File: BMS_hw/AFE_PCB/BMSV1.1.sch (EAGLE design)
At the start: 272 parts, among them IC1 MC33771BEP, IC2 SFH6156-1, IC3 MIC28515V1, IC4 FOD8384-COC, IC5 FOD8384-COC, IC6 FOD8384-COC, IC7 SFH6156-1, IC8 SFH6156-1, Q1 IRLML5203, Q2 IRLML5203, T1 IPT020N10N3V1, T2 IPT020N10N3V1, T3 IPT020N10N3V1, T4 IPT020N10N3V1, U1 NCP1117LP-PG, U2 NCP1117LP-PG, X5 22-23-2041

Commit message: itt@21
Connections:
- net CB_14+/14_C: now also C63.2, C64.2, C80.2, C86.2, IC3.VIN, IC3.VIN@1, IC3.VIN@2, IC3.VIN@3, IC3.VIN@4, IC3.VIN@5, IC3.VIN@6, R79.1
- net VIN: no longer C63.2, C64.2, C80.2, C86.2, IC3.VIN, IC3.VIN@1, IC3.VIN@2, IC3.VIN@3, IC3.VIN@4, IC3.VIN@5, IC3.VIN@6, R79.1

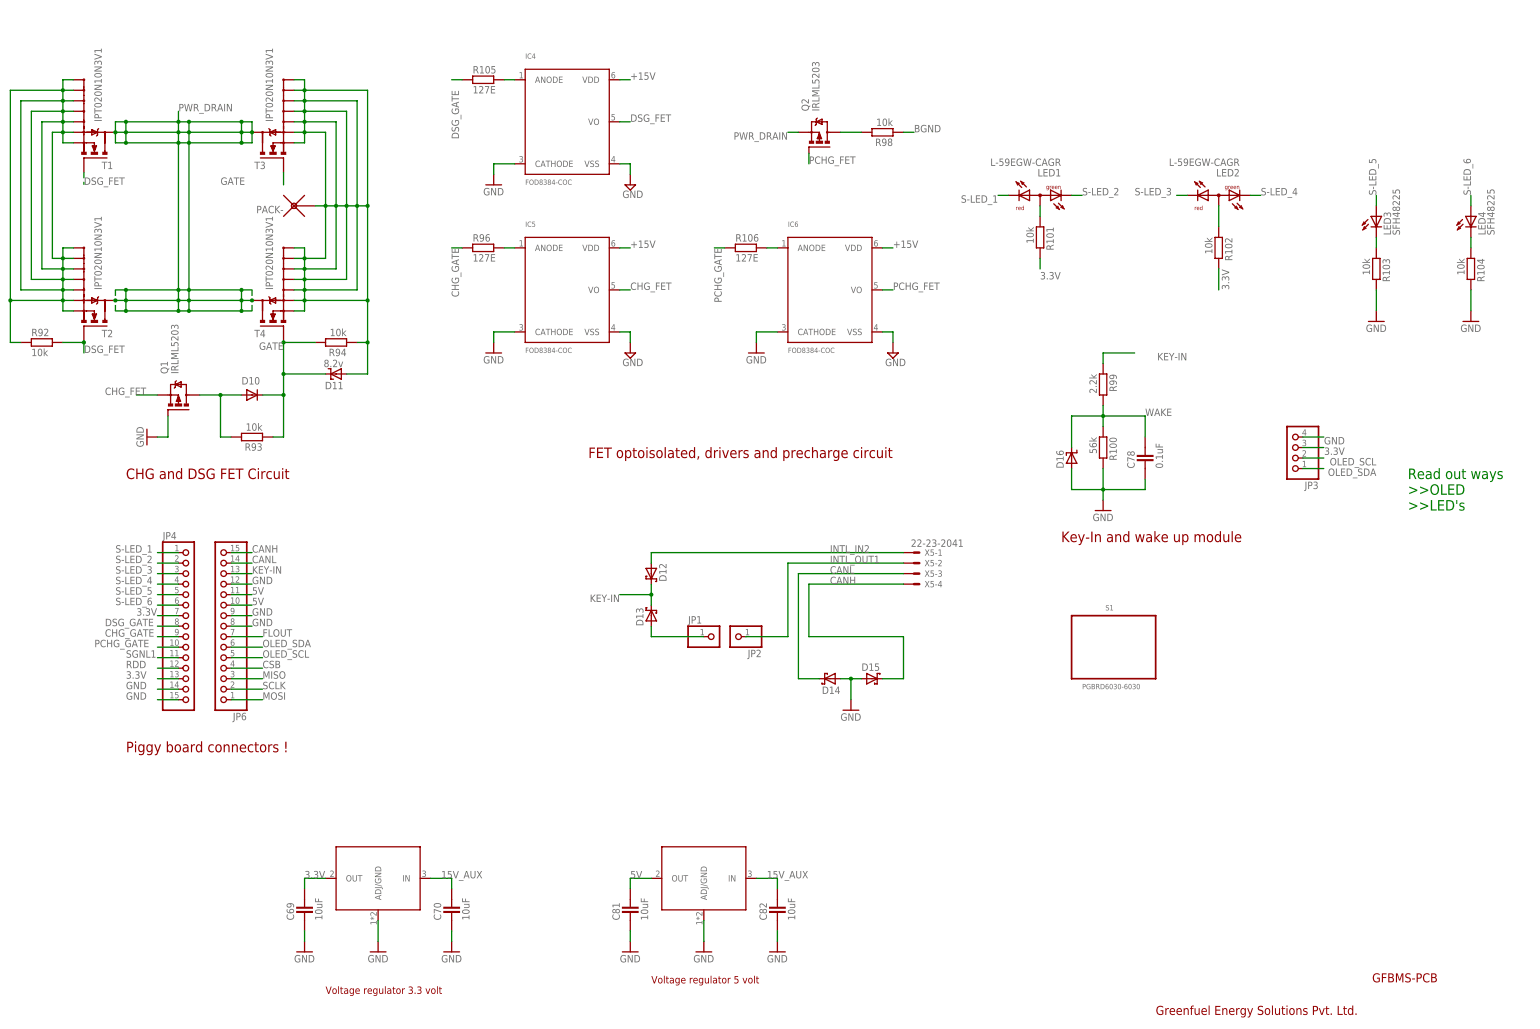
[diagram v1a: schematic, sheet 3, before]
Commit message: updated sch with diff AFE version1.1
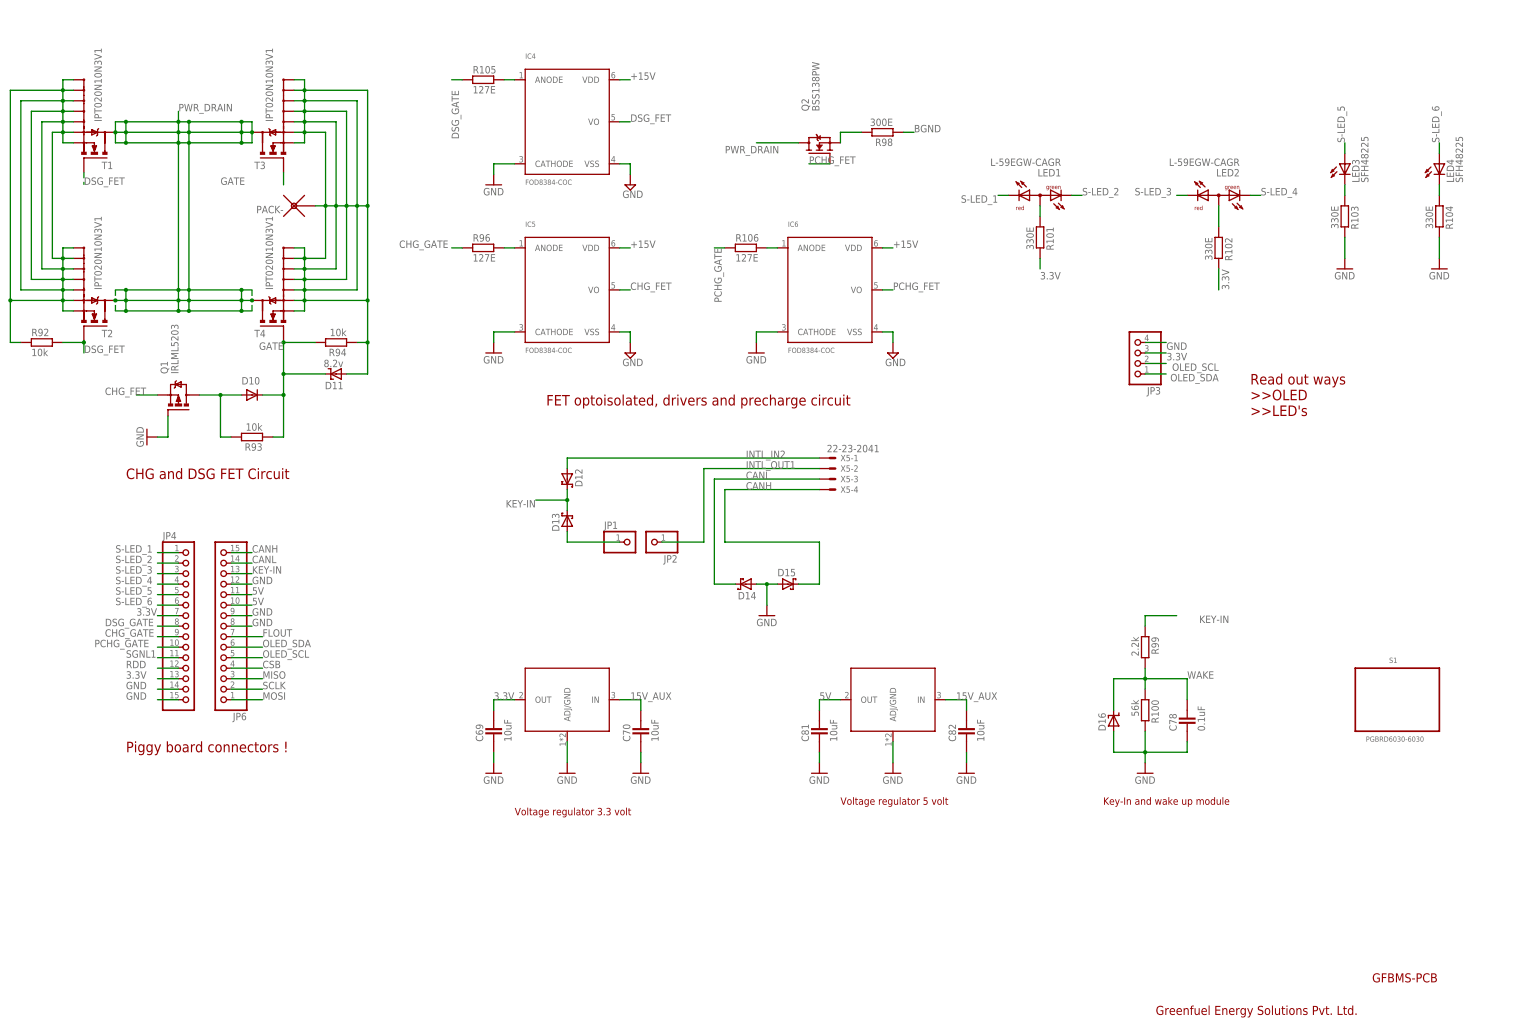
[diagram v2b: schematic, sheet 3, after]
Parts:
- added C90: 39uF 100V, ipc-7351-capacitor:POLARISED_CASE_B
- added C91: 330uF 25V, ipc-7351-capacitor:POLARISED_CASE_B
- Q2: value IRLML5203 -> BSS138PW; device transistor-power:IRLML5203 -> simpa:BSS138PW
- R101, R102, R103, R104: value 10k -> 330E
- R98: value 10k -> 300E
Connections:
- removed net SGNL: D21.A
- net CB_14+/14_C: now also C90.+, IC7LED.K
- net GND: now also C90.-, C91.-, D21.A; no longer IC7LED.K
- net N$28: now also Q2.S; no longer Q2.D
- net PWR_DRAIN: now also Q2.D; no longer Q2.S
- net VCC: now also C91.+
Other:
- moved on the sheet: C69, C70, C78, C81, C82, D12, D13, D14, D15, D16, JP1, JP2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

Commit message: replace part with fod8384 with tlp152 added datasheet in doc folder
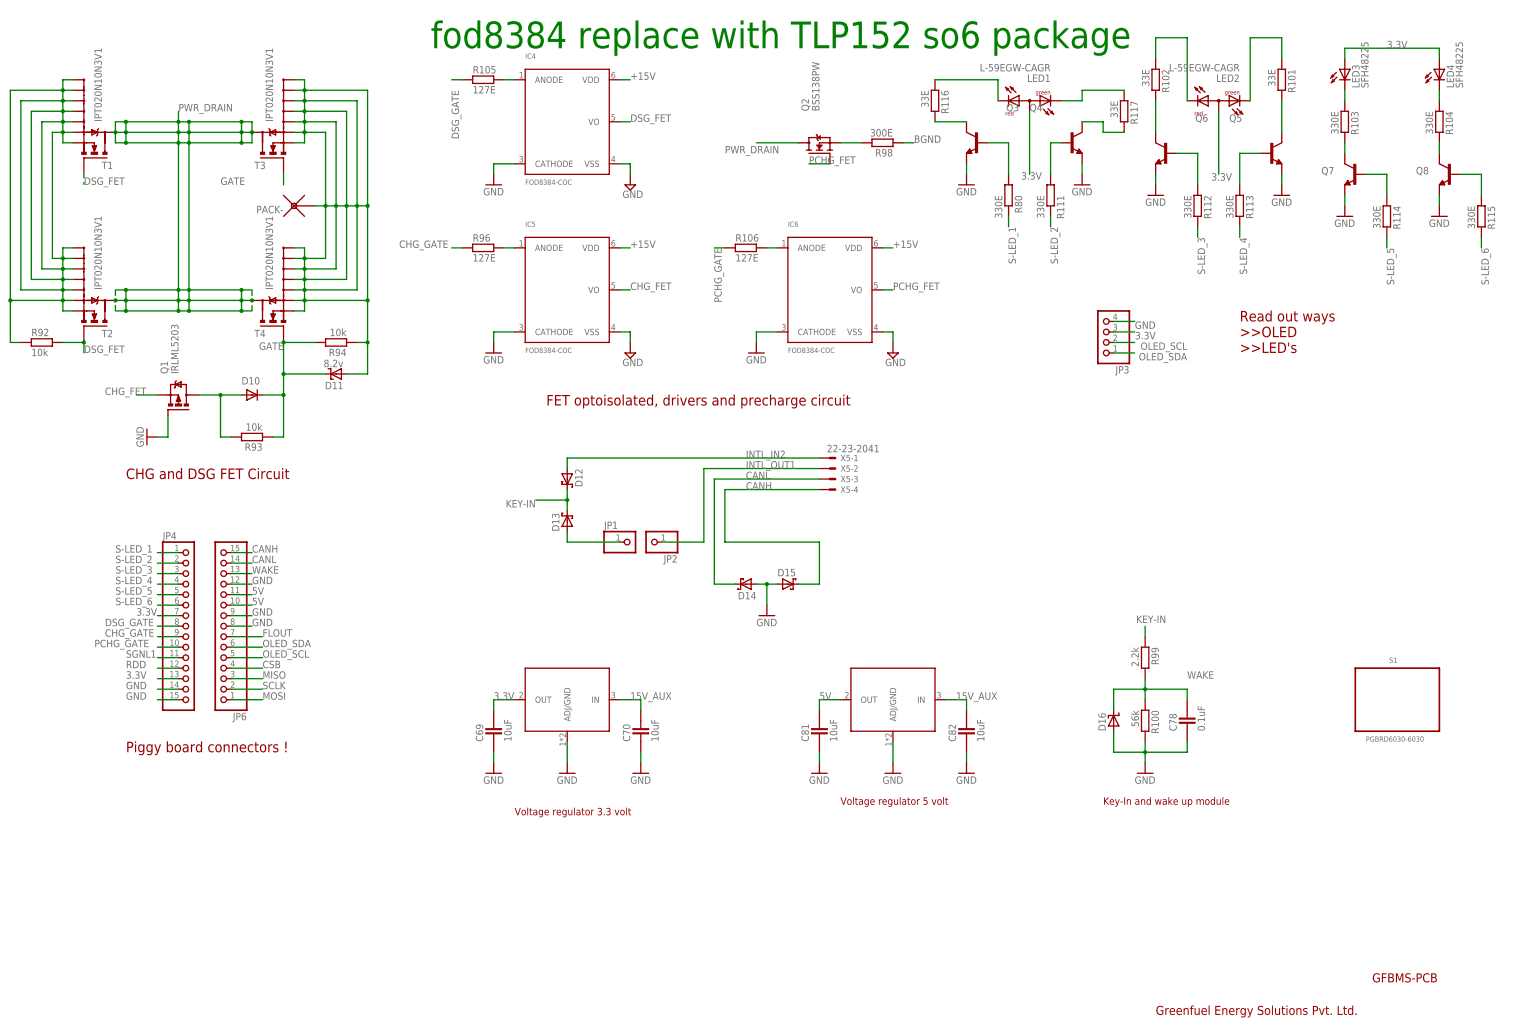
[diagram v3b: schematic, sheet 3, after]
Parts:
- removed C80, C86: 2.2uF 100V, ipc-7351-capacitor:CAPACITOR_1210
- added Q3, Q4, Q5, Q6, Q7, Q8: (no value), ipc-7351-transistor:NPN_SOT-23
- added R111, R112, R113, R114, R115: 330E, ipc-7351-resistor:RESISTOR_0402
- added R116, R117: 33E, ipc-7351-resistor:RESISTOR_0402
- added R118: 0E, ipc-7351-resistor:RESISTOR_0402
- C66: value 47nF -> 0.1uF 100V
- C73: value 1uF -> 2.2uF 16V
- C78: device ipc-7351-capacitor:CAPACITOR_0402 -> ipc-7351-capacitor:CAPACITOR_0603
- C81, C82: device ipc-7351-capacitor:CAPACITOR_0603 -> ipc-7351-capacitor:CAPACITOR_0402
- D16: device ipc-7351-diode:ZENER_SOD-123 -> ipc-7351-diode:ZENER_SOD-323
- R101, R102: value 330E -> 33E
- R66: value 10 -> 10R; device ipc-7351-resistor:RESISTOR_0402 -> ipc-7351-resistor:RESISTOR_0603
- R7: value 100 -> 39E
- R79: value 127E -> 2E
- R80: value 1.6k -> 330E; device ipc-7351-resistor:RESISTOR_0603 -> ipc-7351-resistor:RESISTOR_0402
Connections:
- removed net N$71: LED1.A, R101.1
- removed net N$74: LED2.A, R102.1
- new net N$22: Q7.C, R103.2
- new net N$29: Q8.C, R104.2
- new net N$32: Q3.B, R80.1
- new net N$37: Q4.B, R111.1
- new net N$39: Q6.B, R112.1
- new net N$40: Q5.B, R113.1
- new net N$42: Q7.B, R114.1
- new net N$43: Q8.B, R115.1
- new net N$44: LED1.CR, R116.1
- new net N$45: Q3.C, R116.2
- new net N$47: LED1.CG, R117.1
- new net N$56: Q6.C, R102.2
- new net N$57: Q5.C, R101.2
- new net N$58: Q4.C, R117.2
- new net N$59: LED2.CR, R102.1
- new net N$60: LED2.CG, R101.1
- new net N$61: IC3.MODE, R118.1
- net 3.3V: now also LED1.A, LED2.A, LED3.A, LED4.A; no longer R101.2, R102.2
- net CB_14+/14_C: no longer C80.2, C86.2
- net GND: now also Q3.E, Q4.E, Q5.E, Q6.E, Q7.E, Q8.E, R118.2; no longer C80.1, C86.1, IC3.MODE, R103.2, R104.2
- net ILIM: no longer R80.1
- net KEY-IN: no longer JP6.13
- net S-LED_1: now also R80.2; no longer LED1.CR
- net S-LED_2: now also R111.2; no longer LED1.CG
- net S-LED_3: now also R112.2; no longer LED2.CR
- net S-LED_4: now also R113.2; no longer LED2.CG
- net S-LED_5: now also R114.2; no longer LED3.A
- net S-LED_6: now also R115.2; no longer LED4.A
- net SW: no longer R80.2
- net WAKE: now also JP6.13
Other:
- note added: "fod8384 replace with TLP152 so6 package"
- moved on the sheet: C87, C90, C91, JP3, LED1, LED2, LED3, LED4, R100, R101, R102, R103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

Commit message: afe and piggy board bom layout and schematic all changed for final only dc-dc convertor replacement required !
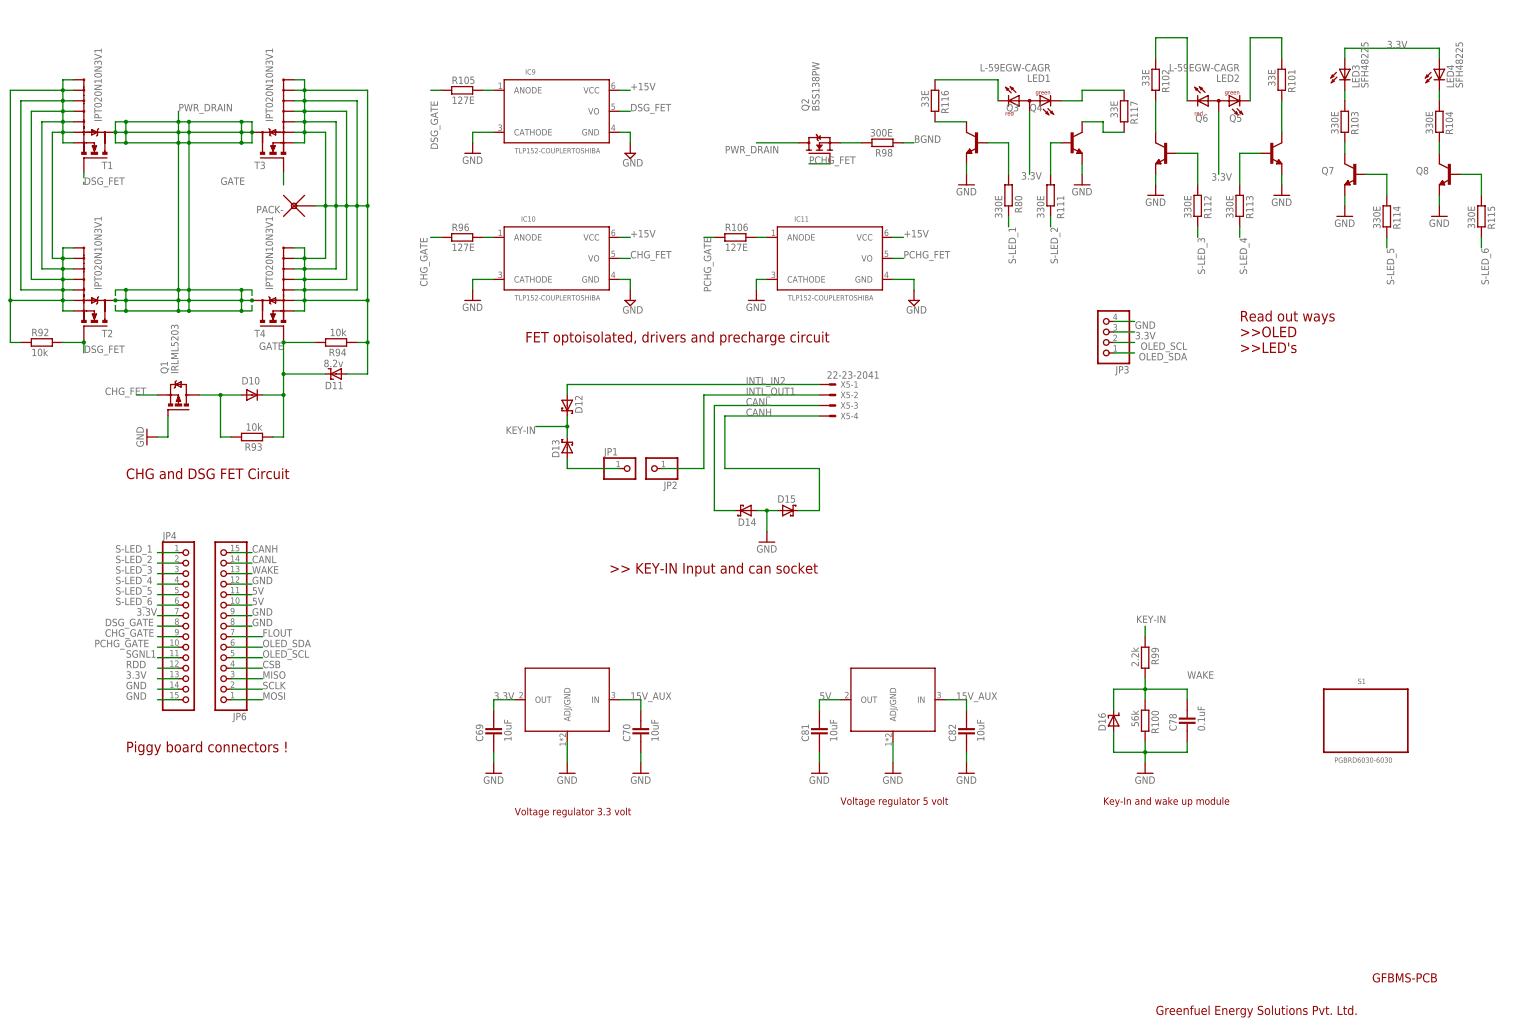
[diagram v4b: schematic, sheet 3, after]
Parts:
- removed IC4, IC5, IC6: FOD8384-COC, GreenFuel:FOD8384-COC
- added IC10, IC11, IC9: TLP152-COUPLERTOSHIBA, GreenFuel:TLP152-COUPLERTOSHIBA
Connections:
- net +15V: now also IC10.VCC, IC11.VCC, IC9.VCC; no longer IC4.VDD, IC5.VDD, IC6.VDD
- net CHG_FET: now also IC10.VO; no longer IC5.VO
- net DSG_FET: now also IC9.VO; no longer IC4.VO
- net GND: now also IC10.CATHODE, IC10.GND, IC11.CATHODE, IC11.GND, IC9.CATHODE, IC9.GND; no longer IC4.CATHODE, IC4.VSS, IC5.CATHODE, IC5.VSS, IC6.CATHODE, IC6.VSS
- net N$20: now also IC9.ANODE; no longer IC4.ANODE
- net N$33: now also IC10.ANODE; no longer IC5.ANODE
- net N$35: now also IC11.ANODE; no longer IC6.ANODE
- net PCHG_FET: now also IC11.VO; no longer IC6.VO
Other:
- note removed: "fod8384 replace with TLP152 so6 package"
- moved on the sheet: C74, C76, D12, D13, D14, D15, JP1, JP2, R105, R106, R118, R91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

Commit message: Afe board updated dc dc convertor
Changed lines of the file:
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@@
 </instance>
 <instance part="C87" gate="G$1" x="309.88" y="114.3" smashed="yes" rot="R180">
-<attribute name="NAME" x="312.42" y="111.76" size="1.778" layer="95" rot="R180"/>
+<attribute name="NAME" x="312.42" y="111.76" size="1.778" layer="95" font="vector" ratio="12" rot="R180"/>
 <attribute name="VALUE" x="302.26" y="116.84" size="1.778" layer="96" font="vector" ratio="12"/>
 </instance>
@@
 </instance>
 <instance part="C91" gate="G$1" x="309.88" y="81.28" smashed="yes" rot="R180">
-<attribute name="NAME" x="312.42" y="79.248" size="1.778" layer="95" rot="R180"/>
+<attribute name="NAME" x="312.42" y="79.248" size="1.778" layer="95" font="vector" ratio="12" rot="R180"/>
 <attribute name="VALUE" x="314.96" y="77.47" size="1.778" layer="96" rot="R180"/>
 </instance>
